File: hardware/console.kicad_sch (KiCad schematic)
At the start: 24 parts, among them J1 5V_USB, J2 4.5V_BAT, J3 SWD, J4 UART, Q1 AO3401A, SW1 SW_LEFT, SW2 SW_RIGHT, SW3 SW_UP, SW4 SW_DOWN, SW5 SW_A, SW6 SW_B, U1 STM32G030C8Tx, U2 XC6206PxxxMR

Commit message: everything with old power supply
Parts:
- removed R3: 100k, symbol Device:R
- added C3, C4: 10u, Capacitor_SMD:C_0805_2012Metric, symbol Device:C
- added C5, C7, C9: 100n, Capacitor_SMD:C_0402_1005Metric, symbol Device:C
- added C6: 4.7u, Capacitor_SMD:C_0603_1608Metric, symbol Device:C
- added C8: 1u, Capacitor_SMD:C_0402_1005Metric, symbol Device:C
- added DS1: HS96L03W2C03, console:OLED-TH_L27.8-W27.2-P2.54_C9900033791, symbol console:OLED_128x64_I2C_4P
- added LS1: HNR-1207PA6.5, console:BUZ-TH_BD12.5-P6.50-D0.9, symbol Device:Buzzer
- added R4, R5: 4.7k, Resistor_SMD:R_0402_1005Metric, symbol Device:R
- added R6: 100, Resistor_SMD:R_0402_1005Metric, symbol Device:R
- C1, C2: footprint (none) -> Capacitor_SMD:C_0402_1005Metric
- D3: value C8598 -> B5819W
- J1: value 5V_USB -> USB-C_Module; footprint Connector_PinHeader_2.54mm:PinHeader_1x02_P2.54mm_Vertical -> Connector_PinHeader_2.54mm:PinHeader_1x06_P2.54mm_Vertical; symbol Connector_Generic:Conn_01x02 -> console:USB_C_Breakout_6P
- J2: footprint (none) -> Connector_JST:JST_PH_S2B-PH-K_1x02_P2.00mm_Horizontal
- Q1: MPN (none) -> AO3401A; Manufacturer (none) -> Alpha & Omega
- R1: value 10k -> 2.2k
- R2: value 1M -> 100k; footprint (none) -> Resistor_SMD:R_0402_1005Metric
- U1: value STM32G030C8Tx -> STM32G030C8T6
- U2: value XC6206PxxxMR -> XC6206P332MR; MPN (none) -> XC6206P332MR-G; Manufacturer (none) -> Torex
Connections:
- net +3.3V: now also D2.2 (A), J3.4 (Pin_4), J4.4 (Pin_4), U1.4 (VBAT), U1.5 (VREF+), U1.6 (VDD), U2.2 (VO), C4.1, C5.1, C6.1, C7.1, C8.1, DS1.2 (VCC), R4.1, R5.1
- net GND: now also J1.2 (GND), J3.1 (Pin_1), J4.1 (Pin_1), U1.7 (VSS), C3.2, C4.2, C5.2, C6.2, C7.2, C8.2, C9.2, DS1.1 (GND), LS1.2 (-); no longer J1.1 (Pin_1)
- net VSYS: now also Q1.2 (S), C3.1; no longer Q1.3 (D)
- net UART_TX: now reaches J4.2 (Pin_2)
- net UART_TX: now also U1.13 (PA2)
- net UART_RX: now reaches J4.3 (Pin_3)
- net UART_RX: now also U1.14 (PA3)
- net BTN_UP: now reaches SW3.1 (A)
- net BTN_UP: now also U1.21 (PB2)
- net USB_5V: now reaches Q1.1 (G), R2.2
- net USB_5V: now also D3.2 (A), J1.1 (VBUS)
- net SWDIO: now reaches J3.2 (Pin_2)
- net SWDIO: now also U1.35 (PA13)
- net SWCLK: now reaches J3.3 (Pin_3)
- net SWCLK: now also U1.36 (PA14)
- net BAT+: now reaches J2.2 (Pin_2)
- net BAT+: now also Q1.3 (D); no longer Q1.2 (S)
- net BTN_DOWN: now reaches SW4.1 (A)
- net BTN_DOWN: now also U1.42 (PB3)
- net BTN_A: now reaches SW5.1 (A)
- net BTN_A: now also U1.43 (PB4)
- net at U1.10 (NRST): now also C9.1
- net BTN_LEFT: now reaches U1.19 (PB0)
- net BTN_LEFT: now also SW1.1 (A)
- net BTN_RIGHT: now reaches U1.20 (PB1)
- net BTN_RIGHT: now also SW2.1 (A)
- net SPK_PWM: now reaches U1.28 (PA8)
- net SPK_PWM: now also R6.1
- net BTN_B: now reaches U1.44 (PB5)
- net BTN_B: now also SW6.1 (A)
- net I2C_SCL: now reaches U1.45 (PB6)
- net I2C_SCL: now also DS1.3 (SCL), R4.2
- net I2C_SDA: now reaches U1.46 (PB7)
- net I2C_SDA: now also DS1.4 (SDA), R5.2
- new net: LS1.1 (+), R6.2
- no-connect marks 0 -> 32
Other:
- note added: "DS1: 0.96" OLED, SSD1315, LCSC C5248080 VCC abs max 3.3V. Rail is XC6206P332 (3.3V +/-2%) = up to 3.366V: zero margin, see notes. I2C addr 0x3C 7-bit (0x78 write), SA0=0 32mA max with the panel fully lit R4/R5 = bus pull-ups; fit as DNP if the module already carries its own."
- note added: "LS1 is a PIEZO buzzer - a capacitive load, not a coil. <=10 mA at 4 kHz / 5 Vpp, so PA8 drives it directly: no transistor and no flyback diode needed. Drive at 4 kHz +/-500 (resonance) for max SPL. R6 only softens the edges so the capacitive inrush does not couple into the 3V3 rail / OLED. 0R is fine. On 3V3 single-ended expect ~3 dB below the 5 Vpp spec. Want it louder: drive TIM1_CH1 (PA8) agai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"
- note added: "Pin usage: * PB6/PB7 = I2C1 SCL/SDA -> DS1 display DMA1 via DMAMUX; PB8/PB9 is the alt pair * PA8 = TIM1_CH1 -> LS1 piezo, direct drive spares: PA6/PA7, PB8/PB9 Buttons: PB0..PB5, active low. Use the internal pull-ups (~40k), no externals. All six read as GPIOB->IDR & 0x3F. Note: PA14 is shared with BOOT0. Safe with the default option bytes (nBOOT_SEL=1)."
- note added: "Powered by either * USB-C module (J1), 5V on VBUS * 3 AAA batteries (J2) USB takes precedence via Q1; no battery charging."
- note removed: "Powered by either * 5V (ext. power source) * 3 AAA batteries"
- moved on the sheet: C1, C2, D2, Q1, R1, U1

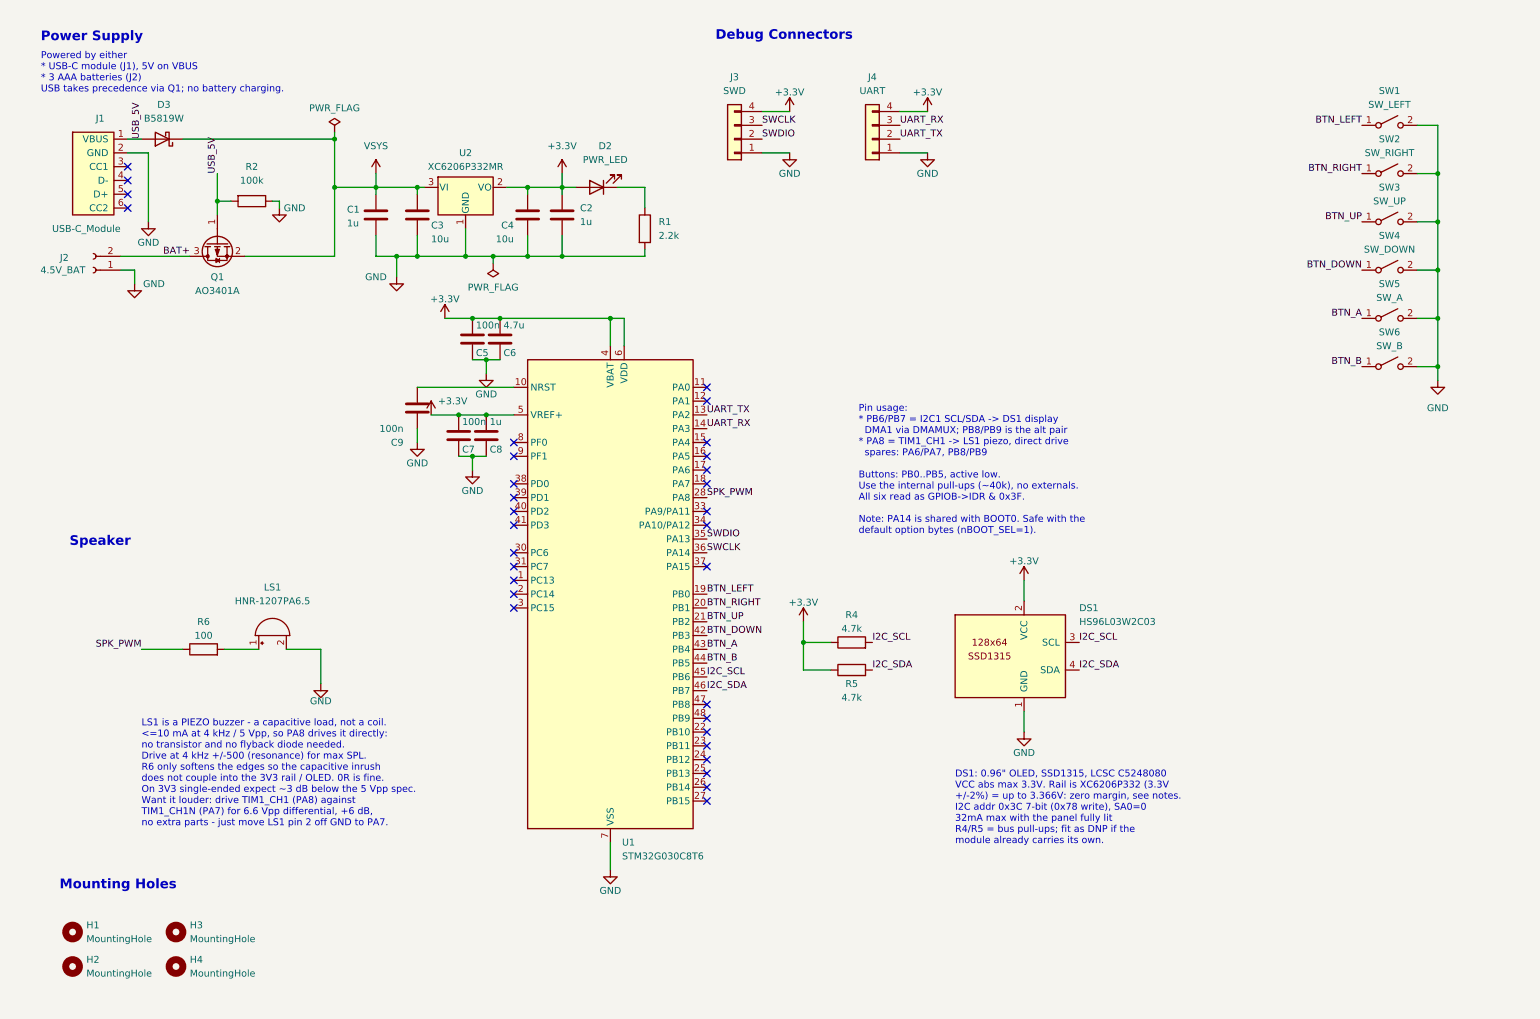
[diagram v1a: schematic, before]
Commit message: move stuff around
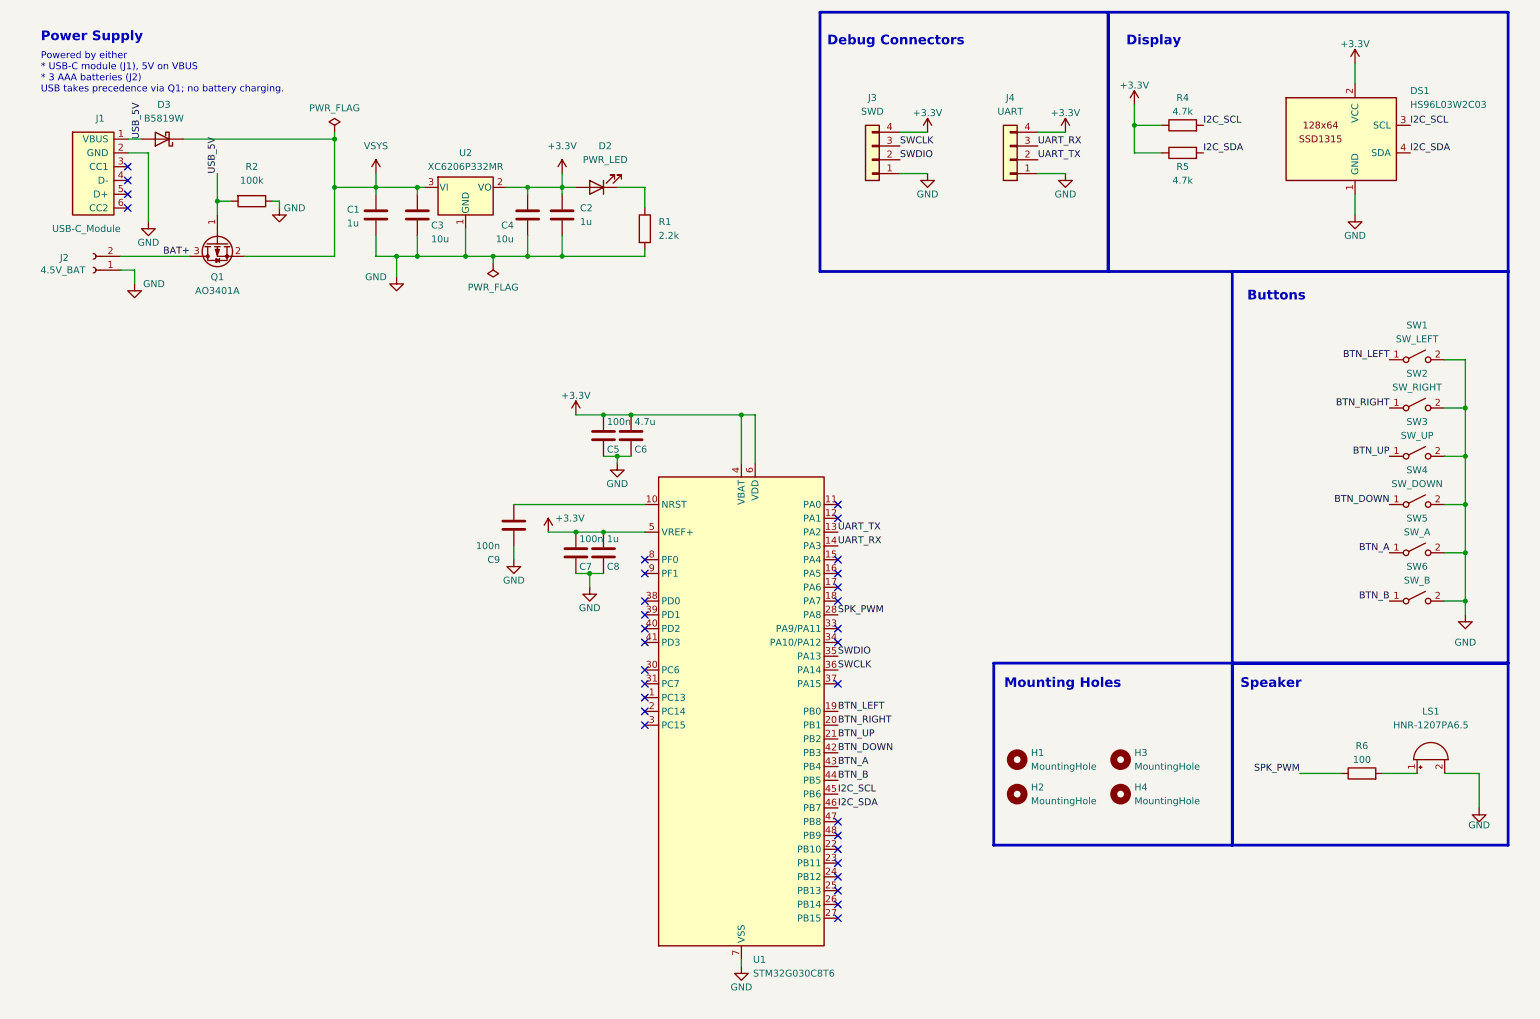
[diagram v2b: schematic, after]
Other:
- note added: "Buttons"
- note added: "Display"
- note removed: "DS1: 0.96" OLED, SSD1315, LCSC C5248080 VCC abs max 3.3V. Rail is XC6206P332 (3.3V +/-2%) = up to 3.366V: zero margin, see notes. I2C addr 0x3C 7-bit (0x78 write), SA0=0 32mA max with the panel fully lit R4/R5 = bus pull-ups; fit as DNP if the module already carries its own."
- note removed: "LS1 is a PIEZO buzzer - a capacitive load, not a coil. <=10 mA at 4 kHz / 5 Vpp, so PA8 drives it directly: no transistor and no flyback diode needed. Drive at 4 kHz +/-500 (resonance) for max SPL. R6 only softens the edges so the capacitive inrush does not couple into the 3V3 rail / OLED. 0R is fine. On 3V3 single-ended expect ~3 dB below the 5 Vpp spec. Want it louder: drive TIM1_CH1 (PA8) agai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"
- note removed: "Pin usage: * PB6/PB7 = I2C1 SCL/SDA -> DS1 display DMA1 via DMAMUX; PB8/PB9 is the alt pair * PA8 = TIM1_CH1 -> LS1 piezo, direct drive spares: PA6/PA7, PB8/PB9 Buttons: PB0..PB5, active low. Use the internal pull-ups (~40k), no externals. All six read as GPIOB->IDR & 0x3F. Note: PA14 is shared with BOOT0. Safe with the default option bytes (nBOOT_SEL=1)."
- moved on the sheet: C5, C6, C7, C8, C9, DS1, H1, H2, H3, H4, J3, J4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

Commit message: checkpoint
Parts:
- removed D2: PWR_LED, LED_SMD:LED_0603_1608Metric, symbol Device:LED
- removed D3: B5819W, Diode_SMD:D_SOD-123, symbol Device:D_Schottky
- removed J2: 4.5V_BAT, Connector_JST:JST_PH_S2B-PH-K_1x02_P2.00mm_Horizontal, symbol Connector:Conn_01x02_Socket
- removed J3: SWD, Connector_PinHeader_2.54mm:PinHeader_1x04_P2.54mm_Vertical, symbol Connector_Generic:Conn_01x04
- removed Q1: AO3401A, Package_TO_SOT_SMD:SOT-23, symbol Transistor_FET:Q_PMOS_GSD
- removed R1: 2.2k, Resistor_SMD:R_0402_1005Metric, symbol Device:R
- removed R2: 100k, Resistor_SMD:R_0402_1005Metric, symbol Device:R
- added C10: 10u, Capacitor_SMD:C_0805_2012Metric, symbol Device:C
- added C11: 1u, Capacitor_SMD:C_0402_1005Metric, symbol Device:C
- added C12: 100n, Capacitor_SMD:C_0402_1005Metric, symbol Device:C
- added D1: CHG, LED_SMD:LED_0603_1608Metric, symbol Device:LED
- added J3: SWD, Connector_PinHeader_2.54mm:PinHeader_1x05_P2.54mm_Vertical, symbol Connector_Generic:Conn_01x05
- added J5: LiPo_140mAh, Connector_JST:JST_PH_B2B-PH-K_1x02_P2.00mm_Vertical, symbol Connector_Generic:Conn_01x02
- added R10, R9: 470k, Resistor_SMD:R_0402_1005Metric, symbol Device:R
- added R7: 16k, Resistor_SMD:R_0402_1005Metric, symbol Device:R
- added R8: 1.5k, Resistor_SMD:R_0402_1005Metric, symbol Device:R
- added U3: TP4054, Package_TO_SOT_SMD:SOT-23-5, symbol console:TP4054
- C1: value 1u -> 100n
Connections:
- net +3.3V: now also J3.5 (Pin_5)
- net GND: now also C10.2, C11.2, C12.2, J3.2 (Pin_2), J5.2 (Pin_2), R10.2, R7.2, U3.2 (GND)
- net SWCLK: now also J3.4 (Pin_4)
- net SWDIO: now also J3.3 (Pin_3)
- net NRST: now reaches C9.1, U1.10 (NRST)
- net NRST: now also J3.1 (Pin_1)
- net VBAT_SENSE: now reaches U1.15 (PA4)
- net VBAT_SENSE: now also C12.1, R10.1, R9.2
- net USB_5V renamed VBUS
- net VBUS: now also C1.1, C10.1, R8.1, U3.4 (VCC)
- net VSYS renamed VBAT_LIPO
- net VBAT_LIPO: now also C11.1, J5.1 (Pin_1), R9.1, U3.3 (BAT); no longer C1.1
- new net: R7.1, U3.5 (PROG)
- new net: D1.2 (A), R8.2
- new net CHG_LED: D1.1 (K), U3.1 (~{CHRG})
- no-connect marks 32 -> 31
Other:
- note added: "Battery gauge: R9/R10 halve VBAT_LIPO into PA4 / ADC_IN4, so VBAT = 2 x V(PA4). Source impedance is 235k, so C12 buffers the ADC sample cap - use a long sampling time (>= 79.5 cycles). Divider draws 4.5uA at 4.2V (~0.08%/day of 140mAh)."
- note added: "Do NOT trust a single readout for the state of charge, do the average of multiple spaced-out readings"
- note added: "FIXME: All these caps seem to be in the "wrong" positions"
- note added: "FIXME: LCSC and footprints for all resistors, caps, LEDs etc"
- note added: "GPIOs all have internal pull-ups"
- note added: "TP4054, by datasheet with I_batt=0.5 * mAh_batt I_batt < 100mA: R_prog=1000/I_batt I_batt >= 100mA: R_prog=1000/I_batt * (1.2 - 4/3 * I_batt)"
- note added: "USB 5V charges the LiPo through U3 and also runs the board. VBAT_LIPO is 3.0-4.2V, so the 3.3V rail drops out below ~3.5V. Use a pack with a built-in protection PCM."
- note removed: "Powered by either * USB-C module (J1), 5V on VBUS * 3 AAA batteries (J2) USB takes precedence via Q1; no battery charging."
- title: (none) -> MicroConsole
- moved on the sheet: C1, C2, C3, C4, C5, C6, C7, C8, C9, DS1, H1, H2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

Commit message: switch
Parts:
- added R1: 0 (DNP), Resistor_SMD:R_0402_1005Metric, symbol Device:R
- added SW7: SW_POWER, console:SW-TH_L8.5-W3.5-P2.50-D0.9, symbol Switch:SW_SPDT
- C2: value 1u -> 10u; footprint Capacitor_SMD:C_0402_1005Metric -> Capacitor_SMD:C_0805_2012Metric
- C4: value 10u -> 1u; footprint Capacitor_SMD:C_0805_2012Metric -> Capacitor_SMD:C_0402_1005Metric
- C5: value 100n -> 4.7u; footprint Capacitor_SMD:C_0402_1005Metric -> Capacitor_SMD:C_0603_1608Metric
- C6: value 4.7u -> 100n; footprint Capacitor_SMD:C_0603_1608Metric -> Capacitor_SMD:C_0402_1005Metric
- C7: value 100n -> 1u
- C8: value 1u -> 100n
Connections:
- net VBAT_LIPO: now also R1.1, SW7.2 (B); no longer C3.1, U2.3 (VI)
- new net VBAT_SW: C3.1, R1.2, SW7.1 (A), U2.3 (VI)
- no-connect marks 31 -> 32
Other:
- note added: "SW7 breaks VBAT_LIPO -> LDO only: the cell still charges with the console switched off. Unused throw (pin 3) is open."
- note removed: "FIXME: All these caps seem to be in the "wrong" positions"
- moved on the sheet: C12, C2, C3, C4, D1, DS1, R10, R4, R5, R8, R9, U2

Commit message: START and SELECT btns
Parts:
- added SW8: SW_START, Button_Switch_SMD:SW_SPST_TS-1088-xR020, symbol Switch:SW_SPST
- added SW9: SW_SELECT, Button_Switch_SMD:SW_SPST_TS-1088-xR020, symbol Switch:SW_SPST
- added TP1: GND, TestPoint:TestPoint_Loop_D2.50mm_Drill1.0mm, symbol Connector:TestPoint
- added TP2: GND, TestPoint:TestPoint_THTPad_D1.5mm_Drill0.7mm, symbol Connector:TestPoint
- added TP3: +3.3V, TestPoint:TestPoint_THTPad_D1.5mm_Drill0.7mm, symbol Connector:TestPoint
- added TP4: VBUS, TestPoint:TestPoint_THTPad_D1.5mm_Drill0.7mm, symbol Connector:TestPoint
- added TP5: VBAT_LIPO, TestPoint:TestPoint_THTPad_D1.5mm_Drill0.7mm, symbol Connector:TestPoint
- added TP6: VBAT_SW, TestPoint:TestPoint_THTPad_D1.5mm_Drill0.7mm, symbol Connector:TestPoint
- added TP7: VBAT_SENSE, TestPoint:TestPoint_THTPad_D1.5mm_Drill0.7mm, symbol Connector:TestPoint
- added TP8: I2C_SDA, TestPoint:TestPoint_THTPad_D1.5mm_Drill0.7mm, symbol Connector:TestPoint
- added TP9: I2C_SCL, TestPoint:TestPoint_THTPad_D1.5mm_Drill0.7mm, symbol Connector:TestPoint
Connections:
- net +3.3V: now also TP3.1
- net GND: now also SW8.2 (B), SW9.2 (B), TP1.1, TP2.1
- net I2C_SCL: now also TP9.1
- net I2C_SDA: now also TP8.1
- net VBAT_LIPO: now also TP5.1
- net VBAT_SENSE: now also TP7.1
- net VBAT_SW: now also TP6.1
- net VBUS: now also TP4.1
- net BTN_START: now reaches U1.47 (PB8)
- net BTN_START: now also SW8.1 (A)
- net BTN_SELECT: now reaches U1.48 (PB9)
- net BTN_SELECT: now also SW9.1 (A)
- no-connect marks 32 -> 30
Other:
- note added: "CHECK: Attempt a pin assignment using STM32CubeMX"
- note added: "CHECK: Differential drive for louder volume?"
- note added: "CHECK: External flash for assets?"
- note added: "Test Points"
- note removed: "Battery gauge: R9/R10 halve VBAT_LIPO into PA4 / ADC_IN4, so VBAT = 2 x V(PA4). Source impedance is 235k, so C12 buffers the ADC sample cap - use a long sampling time (>= 79.5 cycles). Divider draws 4.5uA at 4.2V (~0.08%/day of 140mAh)."
- moved on the sheet: H1, H2, H3, H4, LS1, R6, SW1, SW2, SW3, SW4, SW5, SW6

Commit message: change mcu
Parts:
- removed U1: STM32G030C8T6, Package_QFP:LQFP-48_7x7mm_P0.5mm, symbol MCU_ST_STM32G0:STM32G030C8Tx
- added R11: 10k, Resistor_SMD:R_0402_1005Metric, symbol Device:R
- added SW10: SW_BOOT0, Button_Switch_SMD:SW_SPST_TS-1088-xR020, symbol Switch:SW_SPST
- added U1: STM32G0B1CBT6, Package_QFP:LQFP-48_7x7mm_P0.5mm, symbol MCU_ST_STM32G0:STM32G0B1CBTx
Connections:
- net +3.3V: now also SW10.2 (B), U1.4 (VBAT), U1.5 (VREF+), U1.6 (VDD)
- net BTN_A: now also U1.43 (PB4)
- net BTN_B: now also U1.44 (PB5)
- net BTN_DOWN: now also U1.42 (PB3)
- net BTN_LEFT: now also U1.19 (PB0)
- net BTN_RIGHT: now also U1.20 (PB1)
- net BTN_SELECT: now also U1.48 (PB9)
- net BTN_START: now also U1.47 (PB8)
- net BTN_UP: now also U1.21 (PB2)
- net GND: now also R11.2, U1.7 (VSS)
- net I2C_SCL: now also U1.45 (PB6)
- net I2C_SDA: now also U1.46 (PB7)
- net NRST: now also U1.10 (PF2)
- net SPK_PWM: now also U1.28 (PA8)
- net SWCLK: now also R11.1, SW10.1 (A), U1.36 (PA14)
- net SWDIO: now also U1.35 (PA13)
- net UART_RX: now also U1.14 (PA3)
- net UART_TX: now also U1.13 (PA2)
- net VBAT_SENSE: now also U1.15 (PA4)
- net USB_DM: now reaches J1.4 (D-)
- net USB_DM: now also U1.33 (PA9/PA11)
- net USB_DP: now reaches J1.5 (D+)
- net USB_DP: now also U1.34 (PA10/PA12)
- no-connect marks 30 -> 28
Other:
- note added: "ATTENTION: This button will only work if the option byte nBOOT_SEL is programmed to 0. This can be done on the very first boot via USB/UART, or any time via SWD"
- note removed: "CHECK: External flash for assets?"
- moved on the sheet: C5, C6, C7, C8, C9
